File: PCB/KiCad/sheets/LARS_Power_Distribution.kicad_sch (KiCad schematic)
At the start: 27 parts, among them J3 XT30, U2 TPS2117DRLR, U3 MIC2039AYM6-TR

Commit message: finish PCB routing
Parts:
- C24, C26: value 1u -> 2u2
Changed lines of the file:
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@@
 			)
 		)
-		(property "Value" "1u"
+		(property "Value" "2u2"
 			(at 52.07 170.18 0)
 			(effects
@@
 			)
 		)
-		(property "Value" "1u"
+		(property "Value" "2u2"
 			(at 100.33 81.28 0)
 			(effects

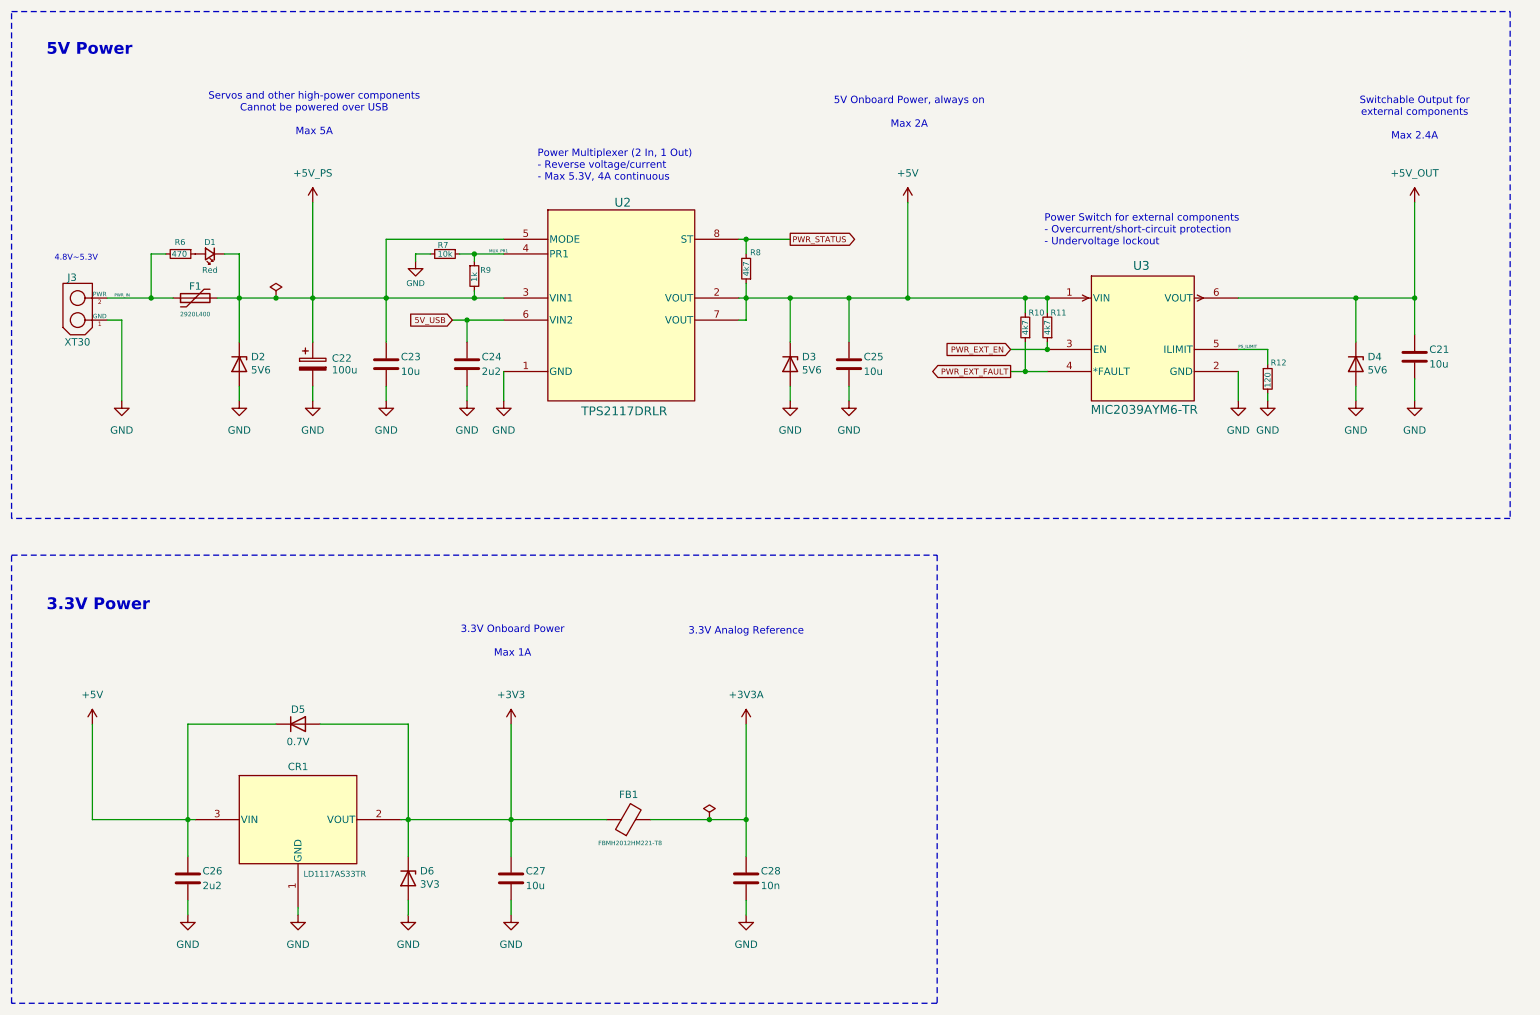
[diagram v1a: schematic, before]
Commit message: change default KiCad schematic font
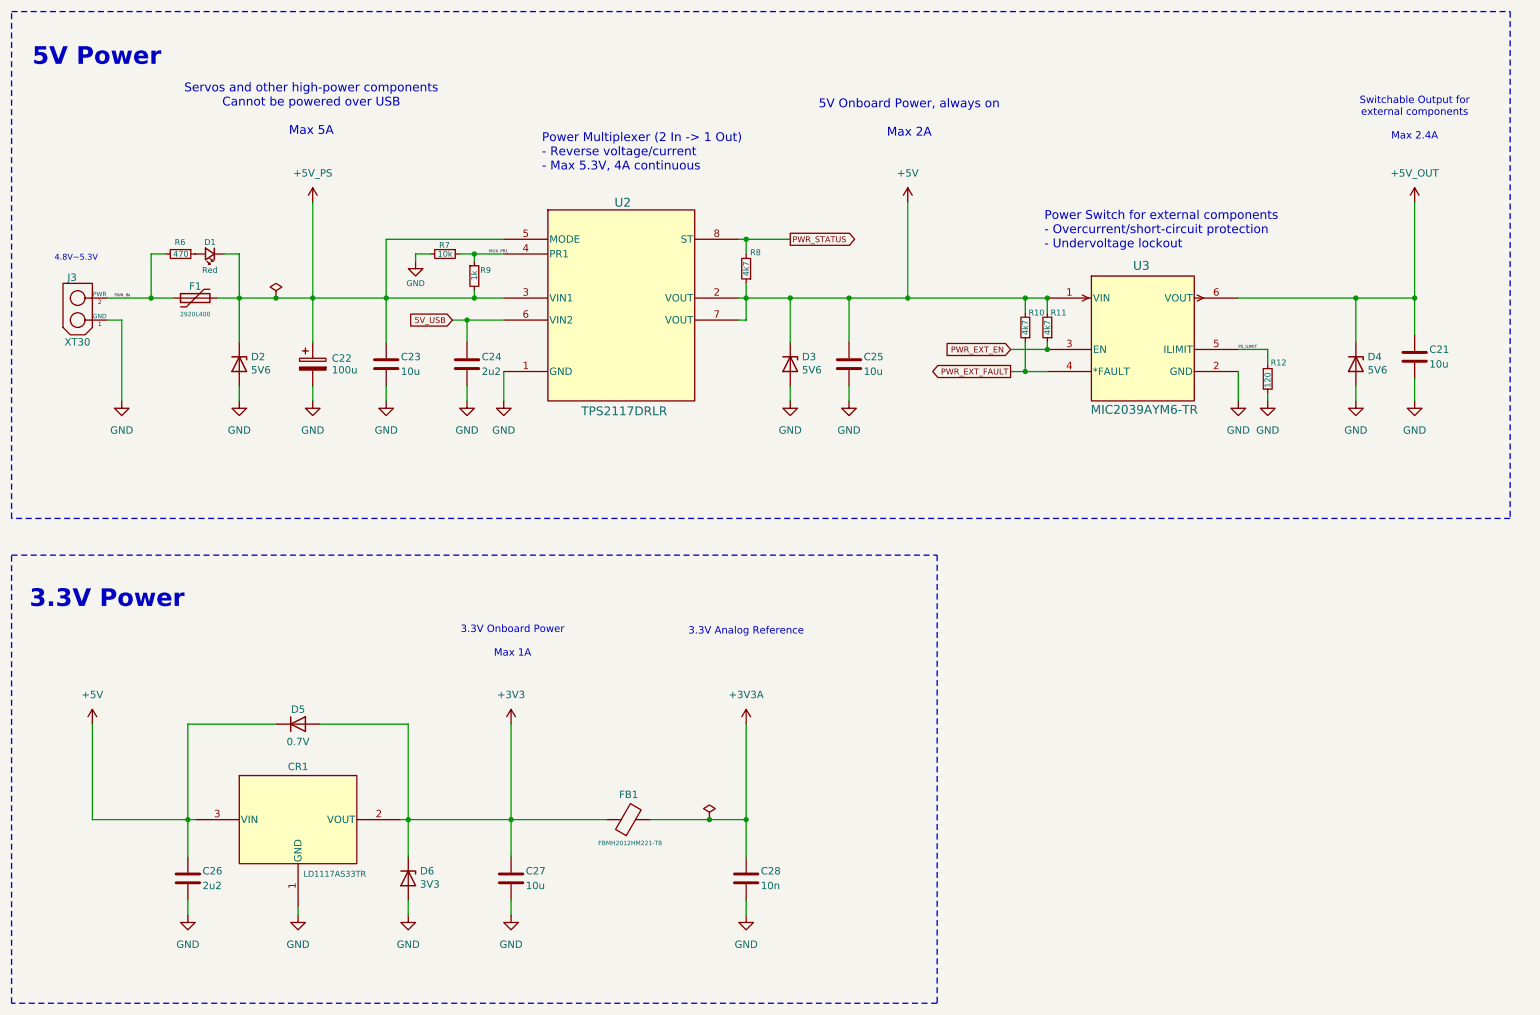
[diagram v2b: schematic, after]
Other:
- note added: "Power Multiplexer (2 In -> 1 Out) - Reverse voltage/current - Max 5.3V, 4A continuous"
- note removed: "Power Multiplexer (2 In, 1 Out) - Reverse voltage/current - Max 5.3V, 4A continuous"
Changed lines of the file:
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@@
 	(text "5V Power\n"
 		(exclude_from_sim no)
-		(at 32.512 25.654 0)
+		(at 33.782 26.924 0)
 		(effects
 			(font
-				(size 2.032 2.032)
+				(size 3.048 3.048)
 				(thickness 0.4064)
 				(bold yes)
@@
 	(text "5V Onboard Power, always on\n\nMax 2A"
 		(exclude_from_sim no)
-		(at 174.244 36.576 0)
+		(at 174.244 37.592 0)
 		(effects
 			(font
-				(size 1.27 1.27)
+				(size 1.524 1.524)
 			)
 		)
 	)
-	(text "Power Multiplexer (2 In, 1 Out)\n- Reverse voltage/current\n- Max 5.3V, 4A continuous"
+	(text "Power Multiplexer (2 In -> 1 Out)\n- Reverse voltage/current\n- Max 5.3V, 4A continuous"
 		(exclude_from_sim no)
-		(at 109.982 45.72 0)
+		(at 110.744 43.434 0)
 		(effects
 			(font
-				(size 1.27 1.27)
+				(size 1.524 1.524)
 			)
 			(justify left)
@@
 	(text "3.3V Power\n"
 		(exclude_from_sim no)
-		(at 34.036 121.666 0)
+		(at 35.56 120.65 0)
 		(effects
 			(font
-				(size 2.032 2.032)
+				(size 3.048 3.048)
 				(thickness 0.4064)
 				(bold yes)
@@
 		(effects
 			(font
-				(size 1.27 1.27)
+				(size 1.524 1.524)
 			)
 			(justify left)
@@
 	(text "Servos and other high-power components\nCannot be powered over USB\n\nMax 5A"
 		(exclude_from_sim no)
-		(at 71.374 36.83 0)
+		(at 70.866 36.068 0)
 		(effects
 			(font
-				(size 1.27 1.27)
+				(size 1.524 1.524)
 			)
 		)
@@
 		)
 		(property "Value" "470"
-			(at 46.736 60.96 90)
+			(at 46.99 60.96 90)
 			(effects
 				(font
@@
 		(dnp no)
 		(property "Reference" "R7"
-			(at 92.71 59.436 90)
+			(at 92.964 59.436 90)
 			(effects
 				(font
@@
 		)
 		(property "Value" "1k"
-			(at 99.06 65.786 90)
+			(at 99.06 65.532 90)
 			(effects
 				(font

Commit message: update text layout and fix remaining DRC errors
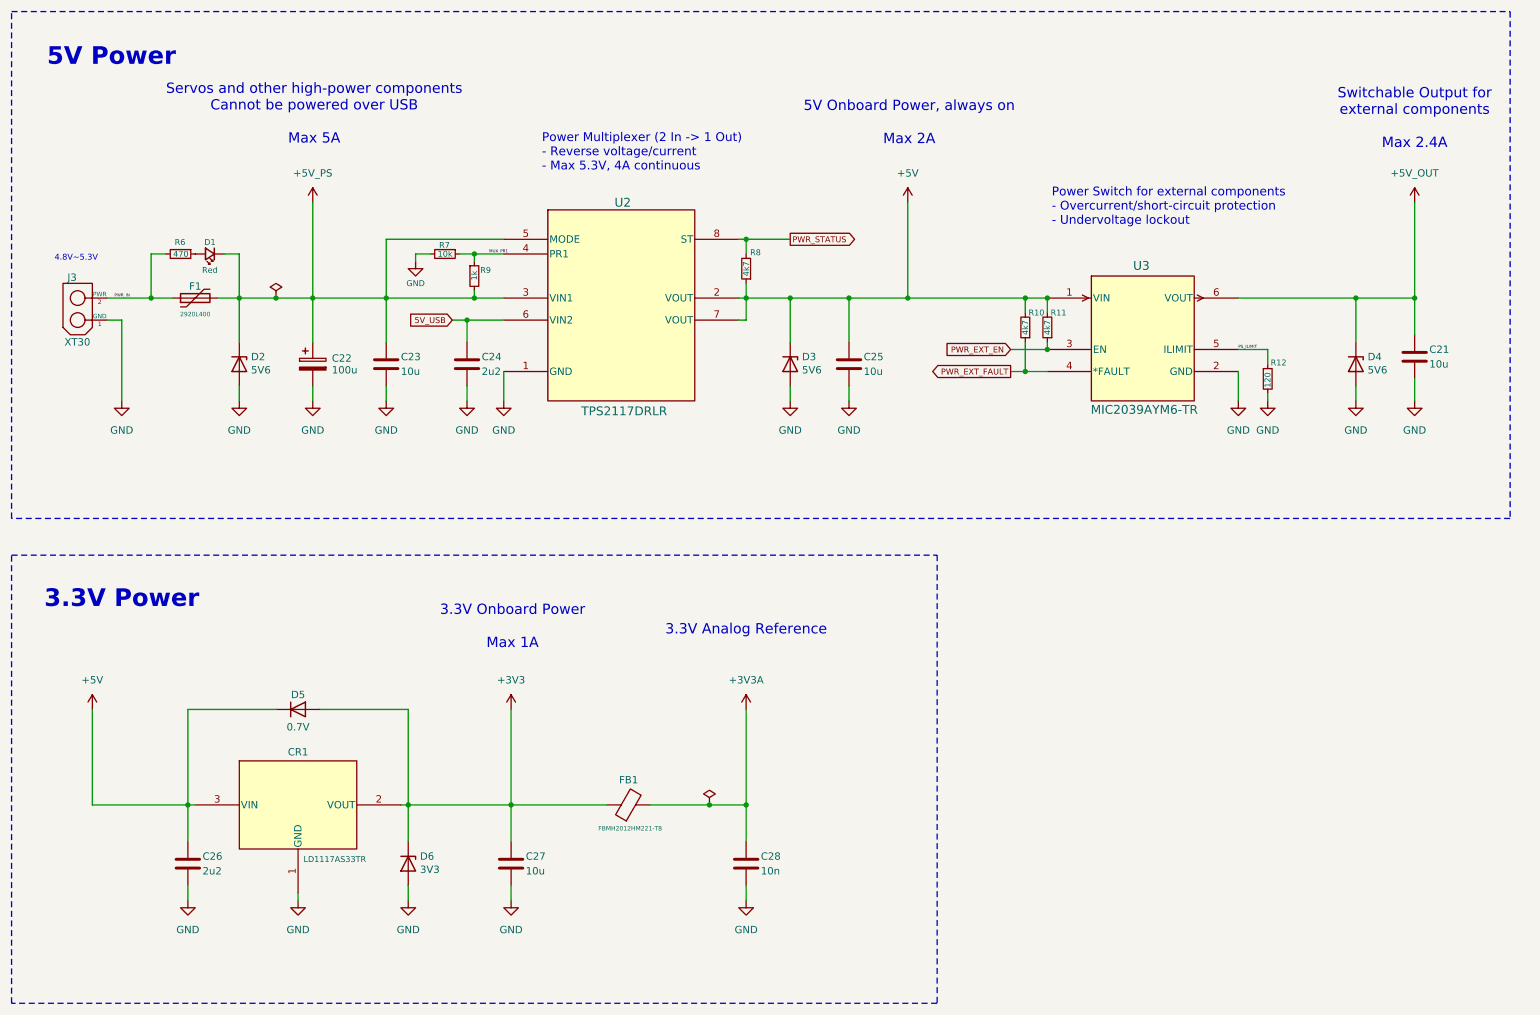
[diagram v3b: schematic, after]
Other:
- moved on the sheet: C26, C27, C28, CR1, D5, D6, FB1

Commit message: add ESD protection and update footprints
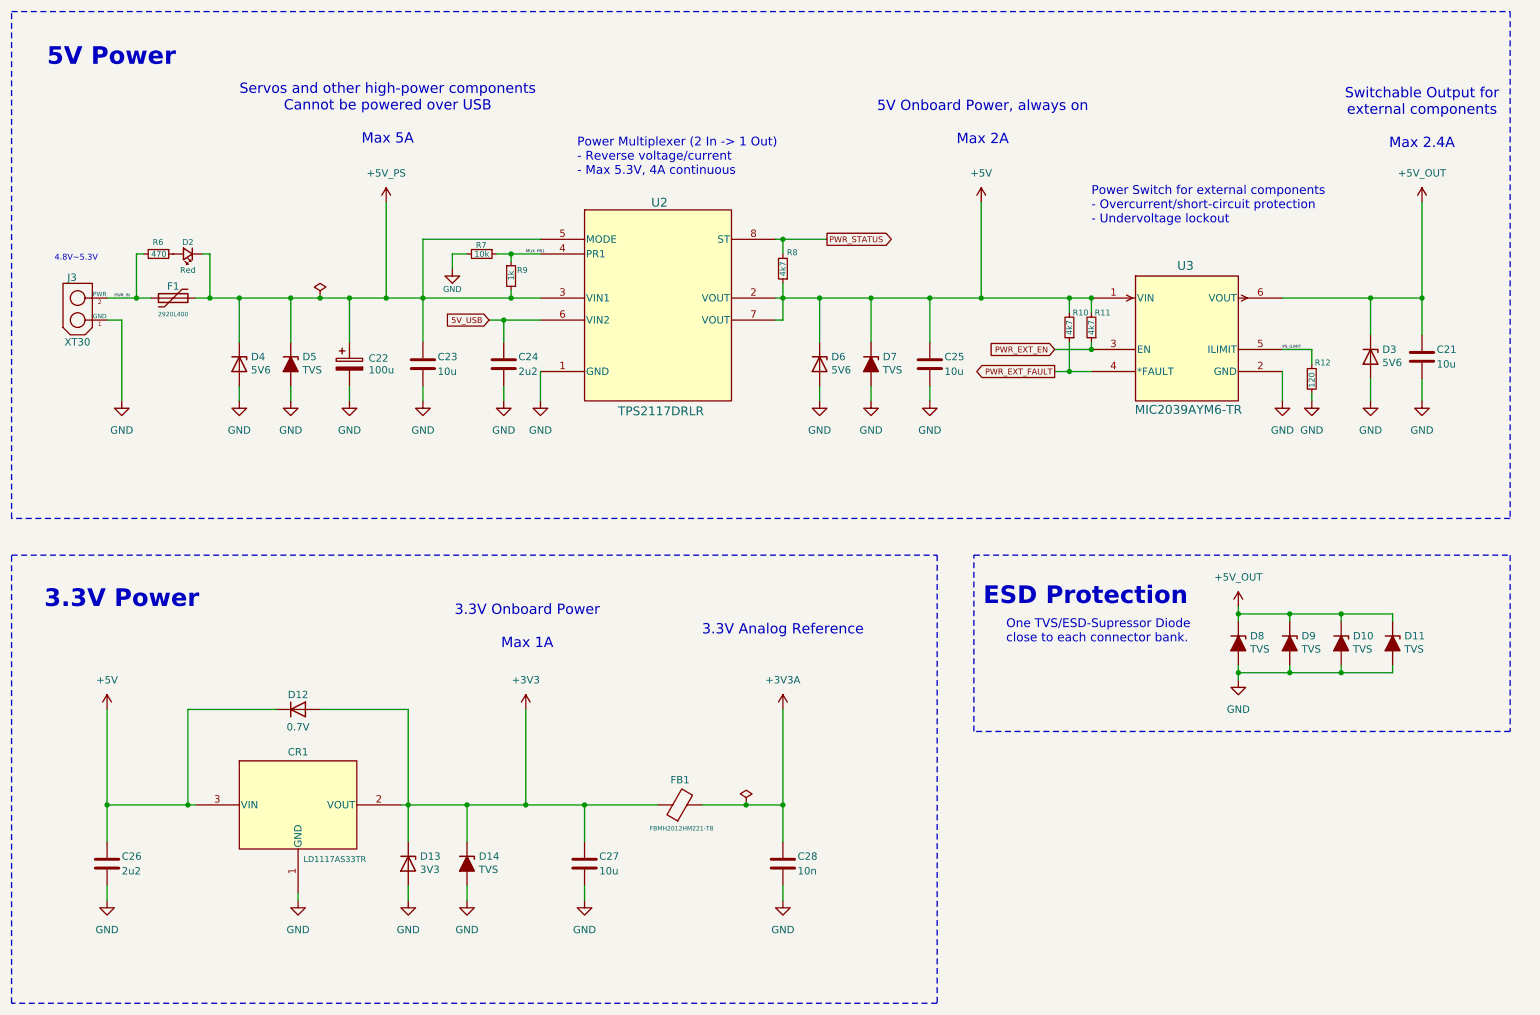
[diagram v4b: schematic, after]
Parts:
- added D10, D11, D14, D5, D7, D8, D9: TVS, LARS_Hardware_Interface:STS321050U182, symbol LARS_Hardware_Interface:D_TVS
- renumbered D5 to D12, D6 to D13, D1 to D2, D4 to D3, D2 to D4, D3 to D6
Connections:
- net +3V3: now also D14.1 (K)
- net +5V: now also D7.1 (K)
- net +5V_OUT: now also D10.1 (K), D11.1 (K), D8.1 (K), D9.1 (K)
- net +5V_PS: now also D5.1 (K)
- net GND: now also D10.2 (A), D11.2 (A), D14.2 (A), D5.2 (A), D7.2 (A), D8.2 (A), D9.2 (A)
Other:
- note added: "ESD Protection"
- note added: "One TVS/ESD-Supressor Diode close to each connector bank."
- moved on the sheet: C21, C22, C23, C24, C25, C26, C27, C28, D2, D3, D6, F1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

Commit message: PCB: update resistor values and embed font
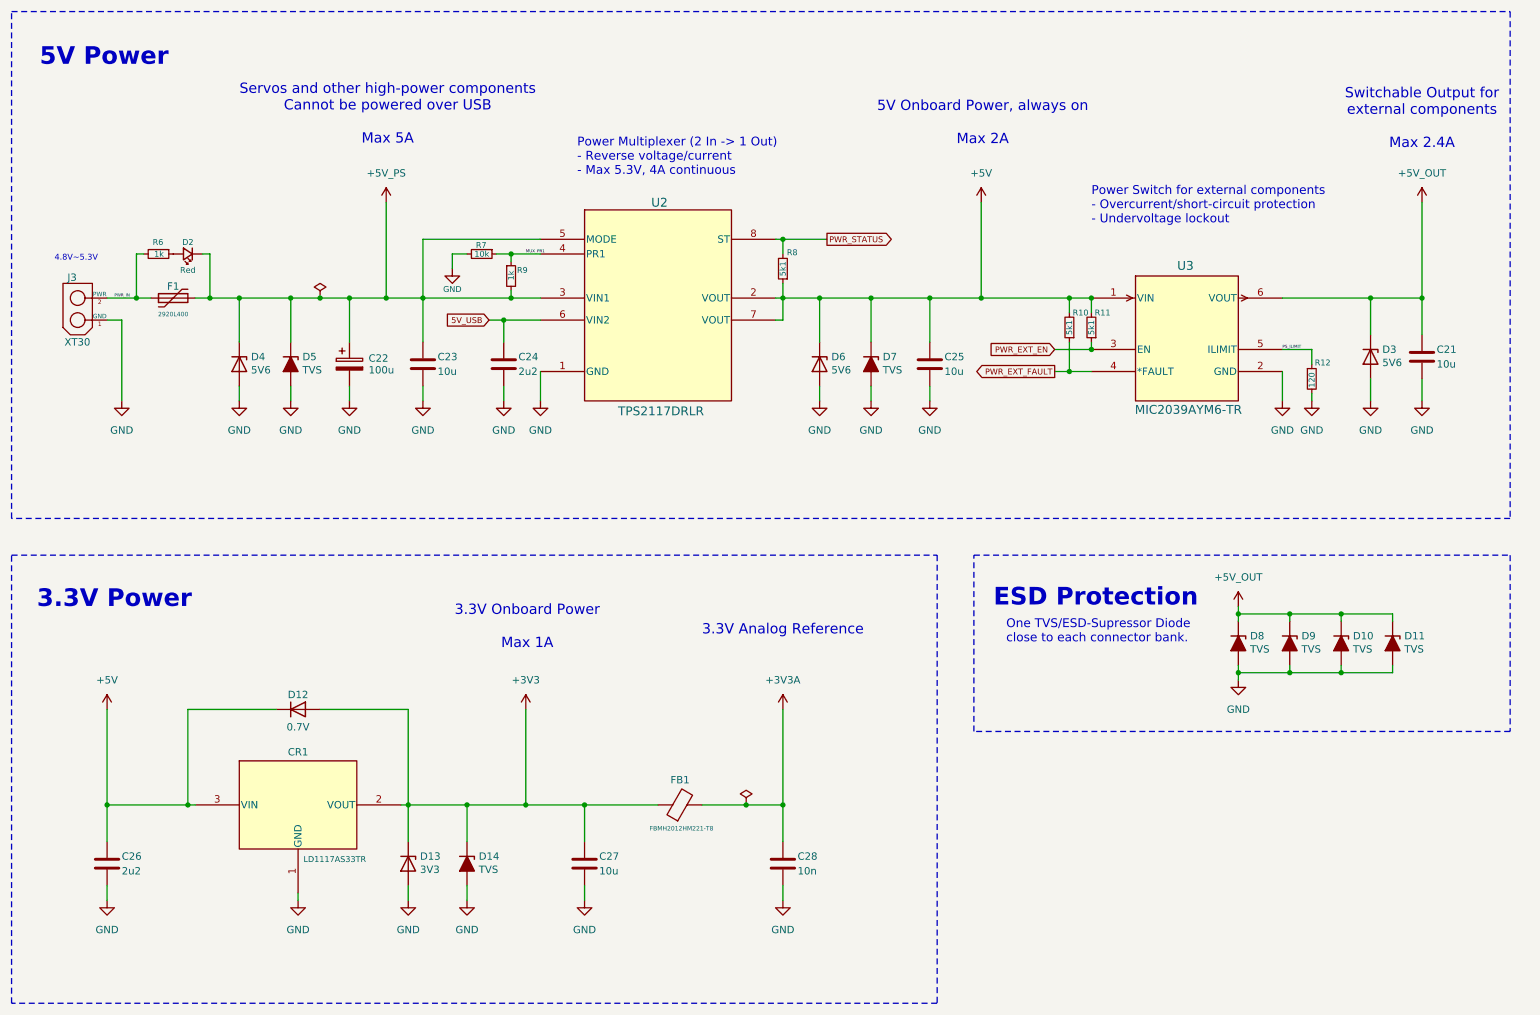
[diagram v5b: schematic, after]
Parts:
- R10, R11, R8: value 4k7 -> 5k1
- R6: value 470 -> 1k
